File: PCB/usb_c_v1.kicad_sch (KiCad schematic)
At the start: 3 parts, among them J4 USB_C_Receptacle_USB2.0_16P

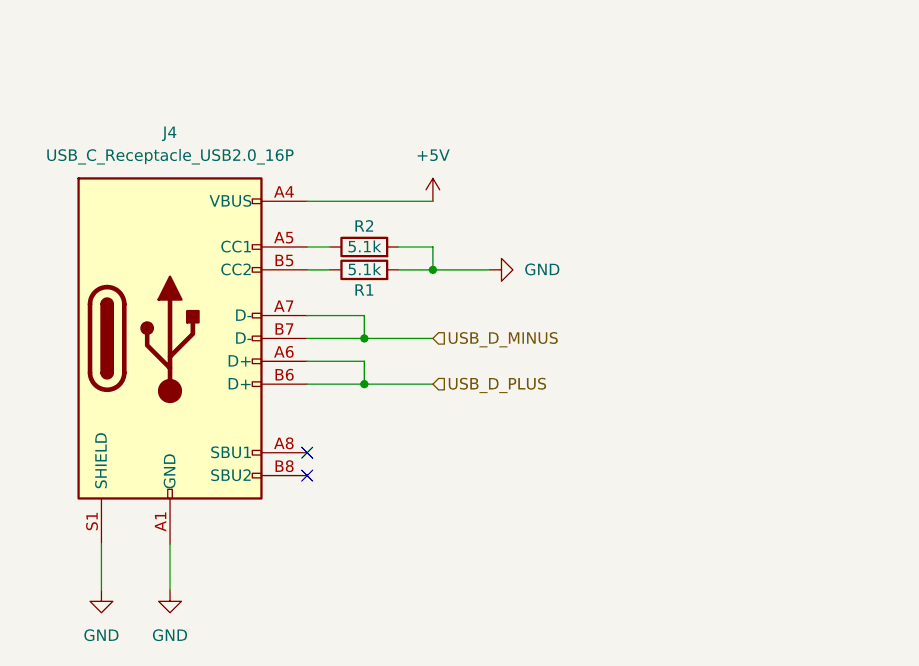
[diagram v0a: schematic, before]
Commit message: added ESD protection to USB-C
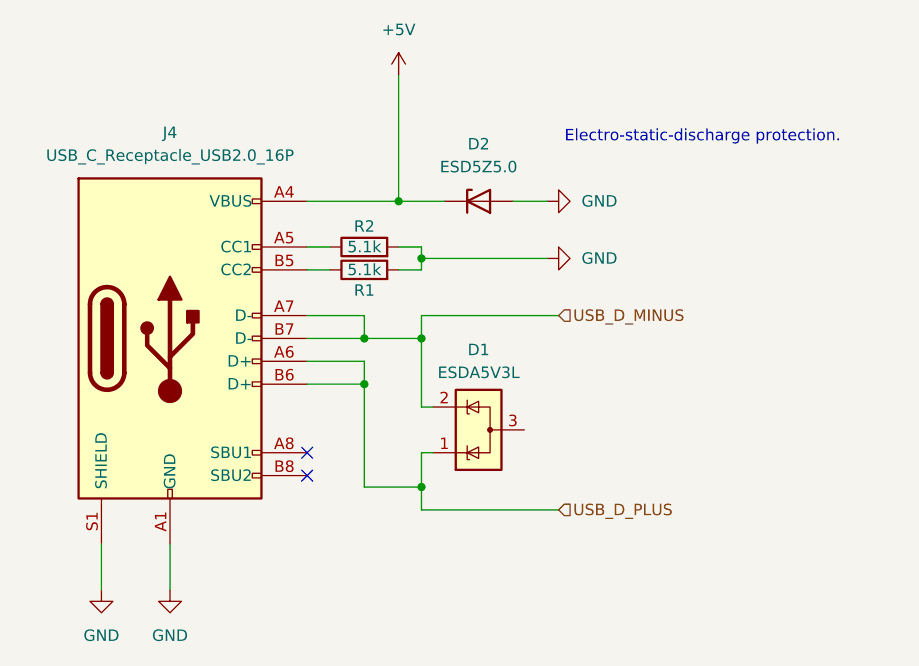
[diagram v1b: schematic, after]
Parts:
- added D1: ESDA5V3L, Package_TO_SOT_SMD:SOT-23-3, symbol Power_Protection:ESDA5V3L
- added D2: ESD5Z5.0, Diode_SMD:D_SOD-523, symbol Diode:ESD5Zxx
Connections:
- net +5V: now also D2.1 (K)
- net GND: now also D2.2 (A)
- net USB_D_MINUS: now also D1.2 (K)
- net USB_D_PLUS: now also D1.1 (K)
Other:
- note added: "Electro-static-discharge protection."

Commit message: added forgotten ground
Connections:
- net GND: now also D1.3 (A)
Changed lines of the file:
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@@
+	(wire
+		(pts
+			(xy 167.64 96.52) (xy 165.1 96.52)
+		)
+		(stroke
+			(width 0)
+			(type default)
+		)
+	)
 	(wire
 		(pts
@@
 		)
 	)
+	(symbol
+		(lib_id "power:GND")
+		(at 167.64 96.52 90)
+		(unit 1)
+		(exclude_from_sim no)
+		(in_bom yes)
+		(on_board yes)
+		(dnp no)
+		(fields_autoplaced yes)
+		(property "Reference" "#PWR06"
+			(at 173.99 96.52 0)
+			(effects
+				(font
+					(size 1.27 1.27)
+				)
+				(hide yes)
+			)
+		)
+		(property "Value" "GND"
+			(at 171.45 96.5199 90)
+			(effects
+				(font
+					(size 1.27 1.27)
+				)
+				(justify right)
+			)
+		)
+		(property "Footprint" ""
+			(at 167.64 96.52 0)
+			(effects
+				(font
+					(size 1.27 1.27)
+				)
+				(hide yes)
+			)
+		)
+		(property "Datasheet" ""
+			(at 167.64 96.52 0)
+			(effects
+				(font
+					(size 1.27 1.27)
+				)
+				(hide yes)
+			)
+		)
+		(property "Description" "Power symbol creates a global label with name \"GND\" , ground"
+			(at 167.64 96.52 0)
+			(effects
+				(font
+					(size 1.27 1.27)
+				)
+				(hide yes)
+			)
+		)
+		(pin "1"
+		)
+		(instances
+			(project "SpinStat"
+				(path "/ffc67360-c592-42dc-bf10-3ceba40203bd/5d22a3c5-a28e-47d3-b10e-f1336e75c38d"
+					(reference "#PWR06")
+					(unit 1)
+				)
+			)
+		)
+	)
